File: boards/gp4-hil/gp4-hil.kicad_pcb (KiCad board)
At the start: 4 copper layers, 160 x 60 mm, 452 parts, among them J1 BEL_FUSE_0826-1G1T-23-F, J2 XILINX_JTAG, J3 XILINX_JTAG_ICESIDE, J4 XILINX_JTAG_ICESIDE, K1 CONN_3_PWROUT, P1 GPAK_ZIF, P2 2x10 HEADER, Q1 SSM6N58NU, Q11 SSM6N58NU, Q12 DMP2069UFY4, Q13 SSM6N58NU, Q14 SSM6N58NU, Q15 SSM6N58NU, Q16 SSM6N58NU, Q17 SSM6N58NU, Q18 SSM6N58NU, Q19 SSM6N58NU, Q20 SSM6N58NU, Q21 SSM6N58NU, Q22 DMP2069UFY4, U1 MIC2288-DFN, U10 AD9609, U11 DAC084S085, U12 DAC084S085, U13 DAC084S085, U14 DAC084S085, U15 TS3A4751, U16 TS3A4751, U17 TS3A4751, U18 TS3A4751, U19 TS3A4751, U2 XC7A100T-1FTG256C, U20 SIP32408, U21 SIP32408, U22 SIP32408, U23 SIP32408, U24 SIP32408, U25 TS3A4751, U26 TS3A4751, U27 TS3A4751, U28 TS3A4751, U29 TXB0104RUT, U3 LTC3374-QFN, U30 TXB0104RUT, U31 ADA4937-2, U32 SIP32408, U33 125 MHz, U34 INA199A2RSW, U35 INA199A2RSW, U36 INA199A2RSW, U4 SIP32408, U5 KSZ9031RN, U6 W25Q32FW, U7 25 MHz, U8 ADG726, U9 AD9609

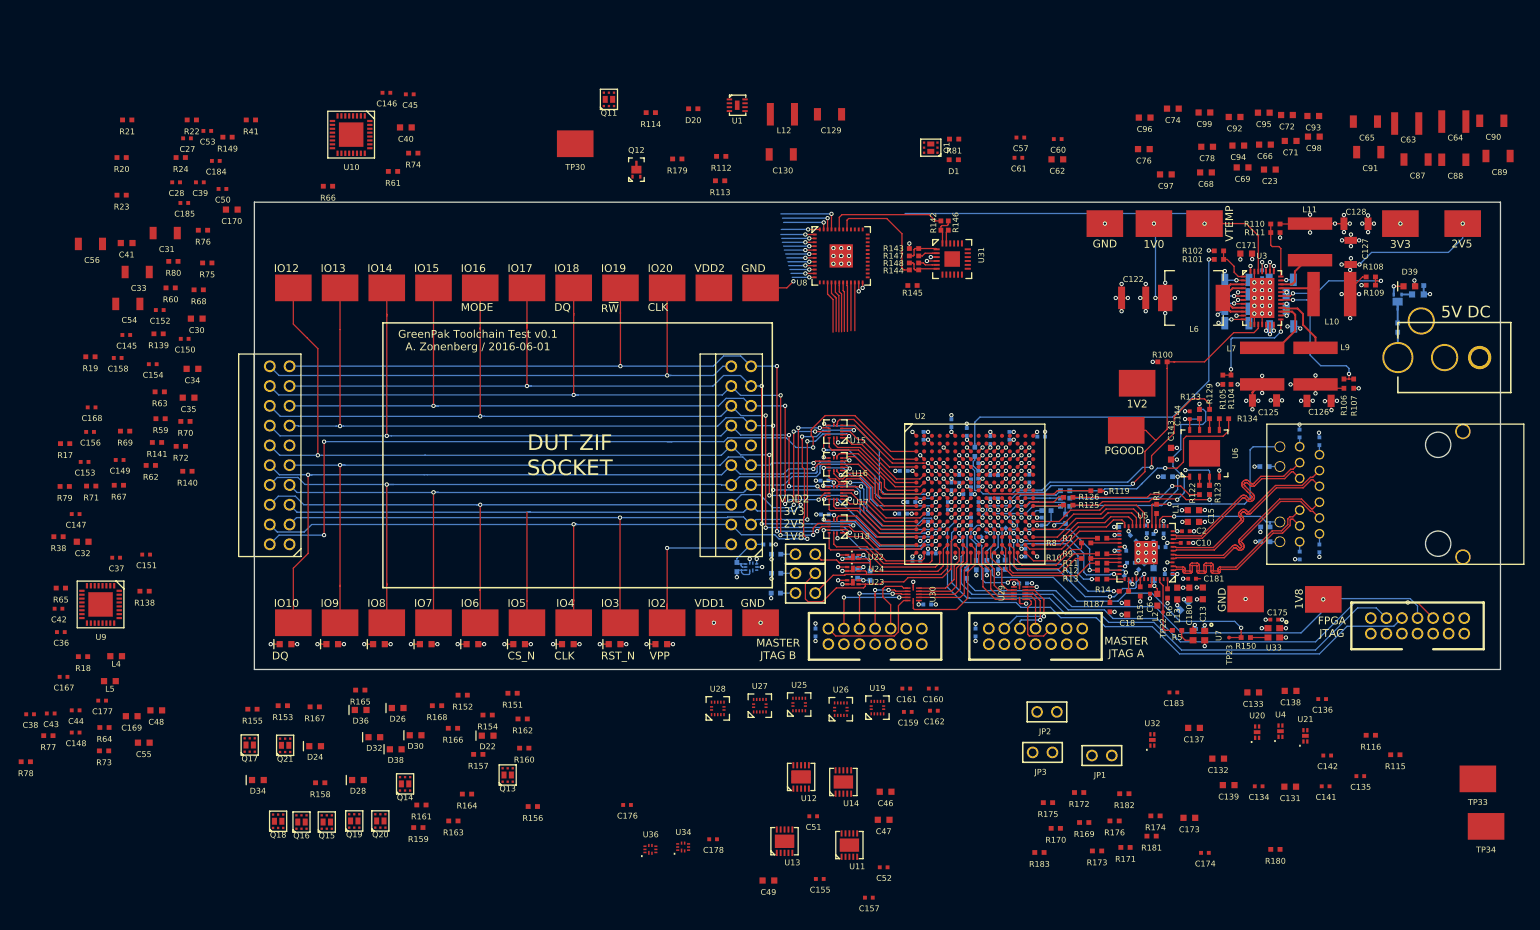
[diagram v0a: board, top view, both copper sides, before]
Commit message: Lots of decoupling capacitor placement
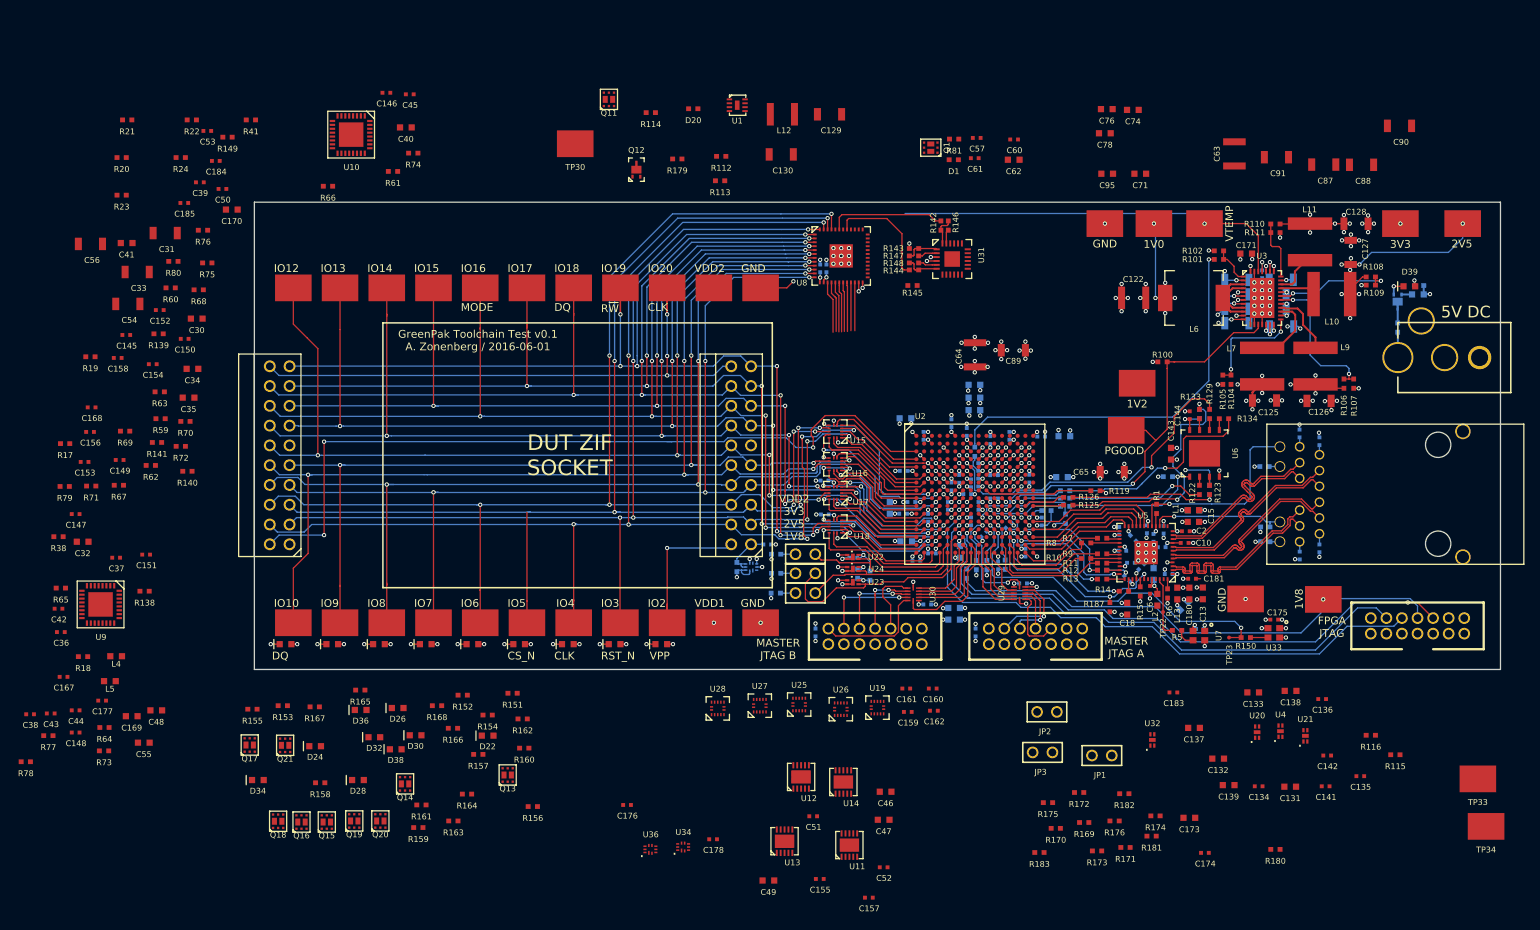
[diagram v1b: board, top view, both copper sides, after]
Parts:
- C23, C27, C28, C66, C68, C69, C72, C92, C93, C94, C96, C97, C98, C99: moved to B.Cu
- moved C28 84.2 mm to (94.5, 68.5), turned to 90 degrees
- moved C27 83.0 mm to (93.7, 68.5), turned to 90 degrees
- moved C92 72.9 mm to (111.6, 112.8), turned to 270 degrees
- moved C98 72.4 mm to (102.6, 99.2), turned to 90 degrees
- moved C96 68.5 mm to (110.1, 112.8), turned to 90 degrees
- moved C64 68.4 mm to (113.5, 79.6), turned to 270 degrees
- moved C89 67.0 mm to (118.5, 79.0)
- moved C94 66.3 mm to (104.7, 103.5)
- moved C68 58.1 mm to (111.6, 104.9), turned to 270 degrees
- moved C65 55.5 mm to (131.2, 94.7)
- moved C99 54.9 mm to (104.6, 87.8)
- moved C72 53.0 mm to (113.5, 83.5)
- moved C93 52.1 mm to (125.0, 90.0)
- moved C66 50.5 mm to (113.5, 86.7)
- moved C69 45.4 mm to (113.5, 85.1), turned to 180 degrees
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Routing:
- net /Analog IO/GND: track 933.1 -> 1006.5 mm, vias 160 -> 183
- net /Analog IO/DUT_GPIO5: track 103.0 -> 158.3 mm, vias 4 -> 6
- net /Analog IO/DUT_GPIO6: track 107.8 -> 162.8 mm, vias 5 -> 7
- net /Analog IO/DUT_GPIO4: track 112.0 -> 167.0 mm, vias 5 -> 7
- net /Analog IO/DUT_GPIO3: track 103.0 -> 155.5 mm, vias 5 -> 7
- net /Analog IO/DUT_GPIO10: track 97.5 -> 135.7 mm, vias 3 -> 5
- net /Analog IO/DUT_GPIO8: track 100.0 -> 136.9 mm, vias 3 -> 5
- net /Analog IO/DUT_GPIO12: track 109.0 -> 145.9 mm, vias 5 -> 7
- net /Analog IO/DUT_GPIO7: track 96.1 -> 132.7 mm, vias 3 -> 5
- net /Analog IO/DUT_GPIO14: track 103.2 -> 139.5 mm, vias 5 -> 7
- net /Analog IO/DUT_GPIO9: track 94.6 -> 130.7 mm, vias 3 -> 5
- net /Analog IO/DUT_GPIO16: track 113.5 -> 149.4 mm, vias 5 -> 7
- net /Analog IO/DUT_GPIO19: track 106.6 -> 142.0 mm, vias 5 -> 7
- net /Analog IO/DUT_GPIO18: track 111.8 -> 146.6 mm, vias 5 -> 7
- net /Analog IO/DUT_GPIO13: track 105.4 -> 139.4 mm, vias 5 -> 7
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
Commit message: Lots of layout on ADC A among other things
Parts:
- C167, C168, C36, C37, C38, C39, Q19, Q20, R138, R139, R151, R153, R155, R157, R159, R161, R163, R165, R167: moved to B.Cu
- R144, R145, R148, R149: value 100K 0.1% -> 10K 0.1%
- moved C38 142.1 mm to (119.8, 63.3), turned to 270 degrees
- moved C36 132.2 mm to (119.0, 66.2)
- moved U9 128.2 mm to (121.0, 65.9), turned to 180 degrees
- moved C169 124.1 mm to (112.3, 63.1)
- moved C167 123.3 mm to (106.9, 66.0), turned to 270 degrees
- moved C37 121.7 mm to (118.9, 67.7)
- moved R138 117.7 mm to (116.0, 65.8), turned to 180 degrees
- moved C168 107.4 mm to (105.9, 68.0), turned to 90 degrees
- moved C39 107.4 mm to (120.8, 68.4), turned to 90 degrees
- moved R139 107.2 mm to (115.8, 73.6), turned to 180 degrees
- moved R149 93.6 mm to (109.0, 71.5), turned to 270 degrees
- moved C170 93.5 mm to (111.0, 71.5)
- moved U10 90.4 mm to (121.0, 73.7), turned to 180 degrees
- moved C178 90.4 mm to (93.8, 52.5)
- moved U34 90.4 mm to (90.0, 53.5)
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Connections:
- Q11 pad G2: /Analog IO/DUT_GPIO9 -> /Analog IO/DUT_GPIO19
- Q18 pad G1: /Analog IO/DUT_GPIO7 -> /Analog IO/DUT_GPIO18
- Q19 pad G1: /Analog IO/DUT_GPIO8 -> /Analog IO/DUT_GPIO7
- Q19 pad G2: /Analog IO/DUT_GPIO18 -> /Analog IO/DUT_GPIO8
- Q20 pad G1: /Analog IO/DUT_GPIO19 -> /Analog IO/DUT_GPIO9
- R161 pad 1: Net-(Q18-PadD1) -> Net-(Q19-PadD1)
- R163 pad 1: Net-(Q19-PadD1) -> Net-(Q19-PadD2)
- R164 pad 1: Net-(Q19-PadD2) -> Net-(Q18-PadD1)
- R165 pad 1: Net-(Q11-PadD2) -> Net-(Q20-PadD1)
- R166 pad 1: Net-(Q20-PadD1) -> Net-(Q11-PadD2)
- U8 pad 29: /Analog IO/PSU_VTEMP -> /Analog IO/ADC_GPIO2
- U8 pad 30: /Analog IO/ADC_GPIO2 -> /Analog IO/ADC_GPIO20
- U8 pad 31: /Analog IO/ADC_GPIO20 -> /Analog IO/ADC_VDD1
- U8 pad 32: /Analog IO/ADC_VDD1 -> /Analog IO/ADC_VDD2
- U8 pad 33: /Analog IO/ADC_VDD2 -> /Analog IO/PSU_VTEMP
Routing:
- net /Analog IO/GND: track 1006.5 -> 1075.0 mm, vias 183 -> 205
- net /Analog IO/A3V3: track 6.83 -> 35.7 mm, vias 5 -> 11
- net /Analog IO/A1V8: track 0.00 -> 14.2 mm, vias 0 -> 4
- net /Analog IO/ADC_B_P: track 0.00 -> 12.2 mm
- net /Analog IO/ADC_B_N: track 0.00 -> 12.0 mm
- net /Analog IO/ADC_B_VCM: track 0.00 -> 11.5 mm, vias 0 -> 2
- net /Analog IO/ADC_A_P: track 0.00 -> 10.2 mm
- net /Analog IO/ADC_A_N: track 0.00 -> 10.2 mm
- net /Analog IO/ADC_A_VCM: track 0.00 -> 8.14 mm, vias 0 -> 2
- net /Analog IO/DUT_GPIO9: track 130.7 -> 138.6 mm, vias 5 -> 6
- net /Analog IO/PSU_VTEMP: track 51.1 -> 58.5 mm, vias 1 -> 2
- net Net-(Q20-PadD2): track 0.00 -> 6.50 mm
- net Net-(Q19-PadD2): track 0.00 -> 4.93 mm
- net Net-(Q19-PadD1): track 0.00 -> 4.88 mm
- net Net-(Q20-PadD1): track 0.00 -> 4.84 mm
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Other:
- board text added: "GreenPak Toolchain Test v0.1 A. Zonenberg / 2016-06-03"
- board text added: "VDD1 3V3 2V5 1V8"
- board text removed: "GreenPak Toolchain Test v0.1 A. Zonenberg / 2016-06-01"

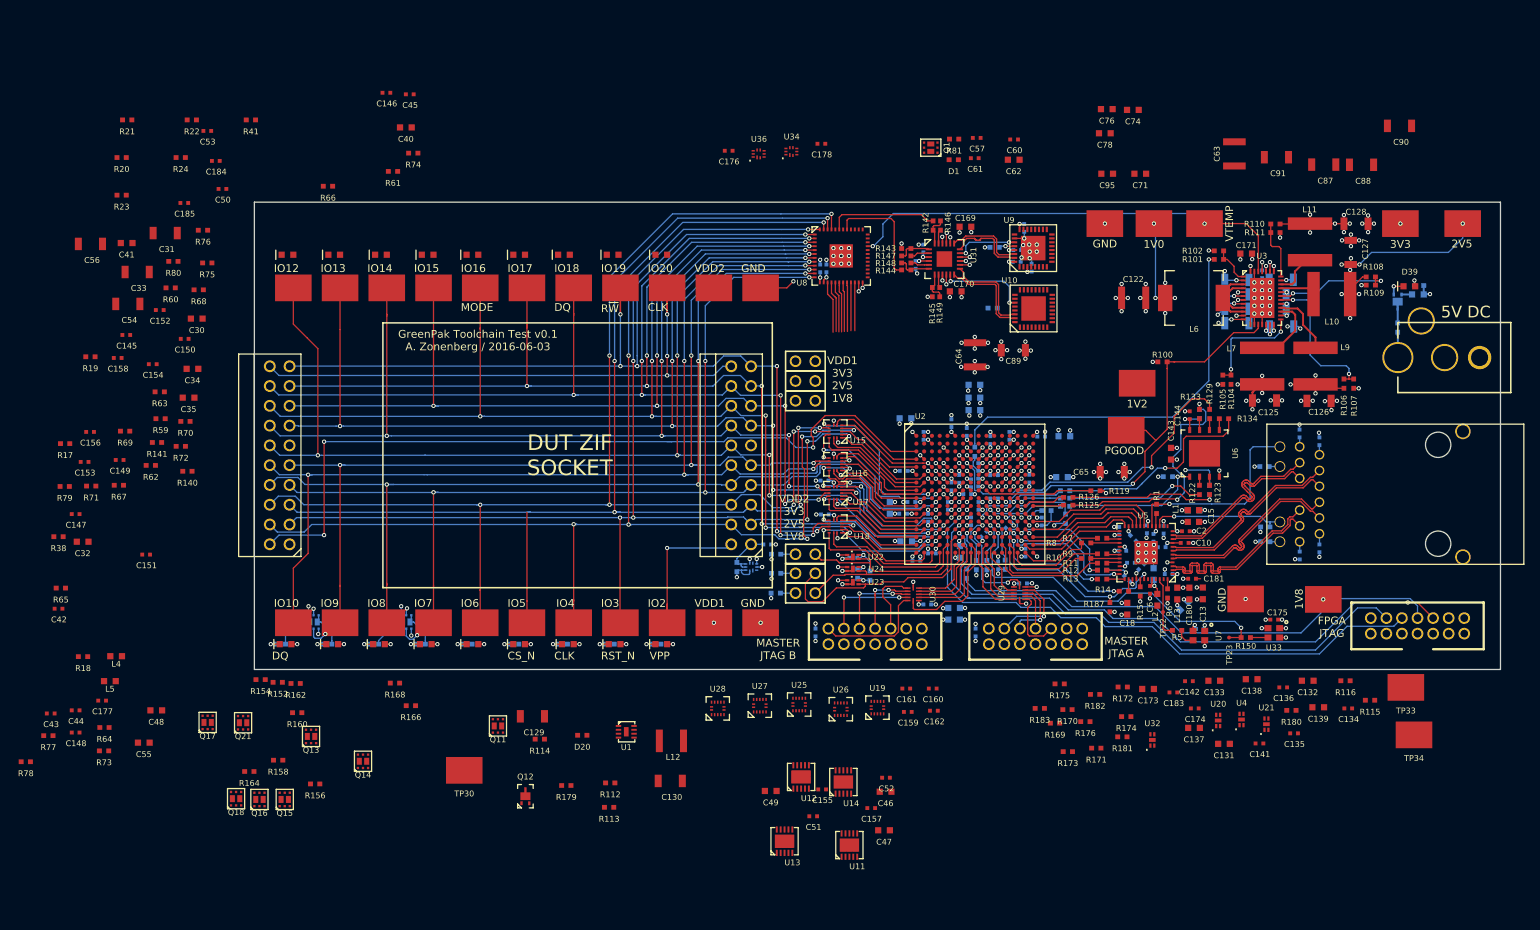
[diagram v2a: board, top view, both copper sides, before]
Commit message: More ADC layout
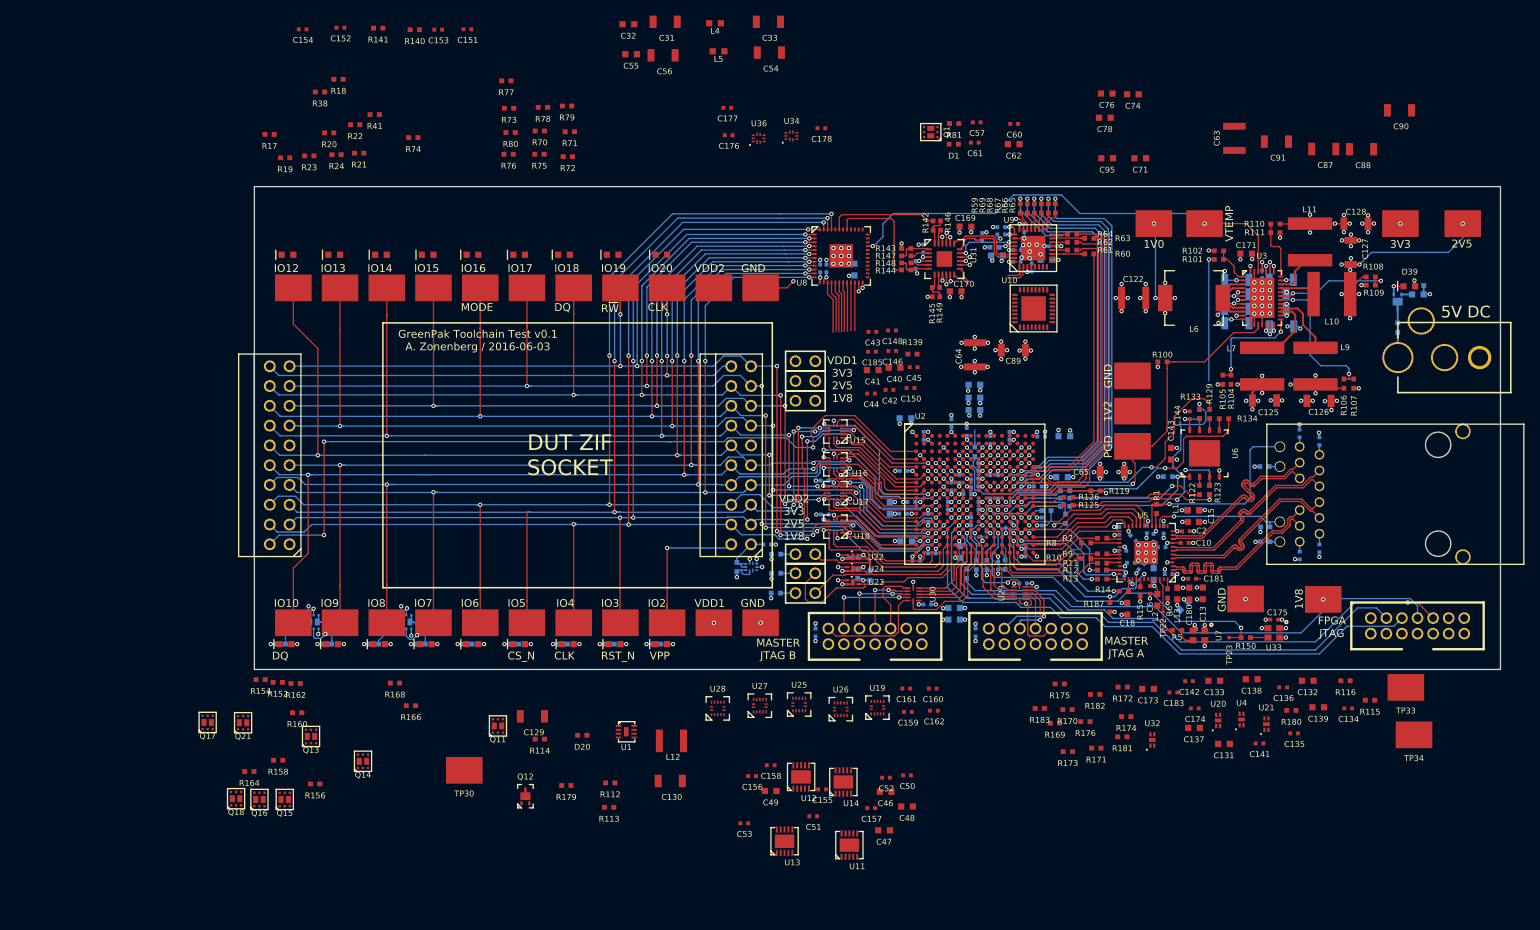
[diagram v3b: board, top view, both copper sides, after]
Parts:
- C145, C147, C149, C184, C30, C34, C35: moved to B.Cu
- R139: moved to F.Cu
- moved R64 139.5 mm to (126.0, 64.1), turned to 180 degrees
- moved R65 136.7 mm to (123.8, 60.8), turned to 270 degrees
- moved C147 124.4 mm to (116.9, 63.2), turned to 180 degrees
- moved R67 123.7 mm to (122.0, 60.8), turned to 270 degrees
- moved R62 121.7 mm to (126.0, 65.2), turned to 180 degrees
- moved R63 121.0 mm to (128.2, 64.7), turned to 180 degrees
- moved R69 119.3 mm to (120.2, 60.8), turned to 270 degrees
- moved R60 118.0 mm to (128.2, 66.7), turned to 180 degrees
- moved C148 116.8 mm to (102.9, 76.5)
- moved C43 116.3 mm to (100.3, 76.7)
- moved C50 115.7 mm to (104.8, 133.6)
- moved C149 114.4 mm to (114.5, 64.5), turned to 90 degrees
- moved R59 113.7 mm to (119.3, 60.8), turned to 270 degrees
- moved C145 113.1 mm to (116.9, 64.2), turned to 180 degrees
- moved C53 112.5 mm to (83.9, 139.8)
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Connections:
- U2 pad A13: /Analog IO/ADC_B_D5 -> Net-(C151-Pad1)
- U2 pad A14: /Analog IO/ADC_B_D6 -> Net-(C152-Pad1)
- U2 pad B16: Net-(C152-Pad1) -> Net-(C154-Pad1)
- U2 pad C16: Net-(C151-Pad1) -> Net-(C153-Pad1)
- U2 pad D11: /Analog IO/ADC_A_D1 -> /Analog IO/DAC_B_DIN
- U2 pad D14: /Analog IO/ADC_A_D2 -> /Analog IO/DAC_SCLK
- U2 pad D15: /Analog IO/ADC_A_D3 -> /Analog IO/DAC_SYNC_N
- U2 pad D16: /Analog IO/ADC_A_D7 -> /Analog IO/ADC_B_D6
- U2 pad E11: /Analog IO/ADC_A_D0 -> /Analog IO/DAC_A_DIN
- U2 pad E15: /Analog IO/ADC_A_D9 -> /Analog IO/ADC_B_D5
- U2 pad E16: /Analog IO/ADC_A_D6 -> /Analog IO/ADC_A_D0
- U2 pad F12: /Analog IO/ADC_A_D4 -> /Analog IO/DAC_D_DIN
- U2 pad F13: /Analog IO/ADC_A_D5 -> /Analog IO/ADC_B_MODE
- U2 pad F14: /Analog IO/DAC_B_DIN -> /Analog IO/ADC_A_D9
- U2 pad F15: /Analog IO/ADC_A_D8 -> /Analog IO/ADC_A_D1
- U2 pad G12: Net-(C154-Pad1) -> /Analog IO/ADC_A_D8
- U2 pad G14: /Analog IO/DAC_C_DIN -> /Analog IO/ADC_A_D7
- U2 pad G15: /Analog IO/DAC_SCLK -> /Analog IO/ADC_A_D2
- U2 pad G16: /Analog IO/DAC_SYNC_N -> /Analog IO/ADC_A_D3
- U2 pad H11: Net-(C153-Pad1) -> /Analog IO/DAC_C_DIN
- U2 pad H13: /Analog IO/DAC_D_DIN -> /Analog IO/ADC_A_D6
- U2 pad H14: /Analog IO/ADC_B_MODE -> /Analog IO/ADC_A_D5
- U2 pad H16: /Analog IO/DAC_A_DIN -> /Analog IO/ADC_A_D4
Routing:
- net /Analog IO/ADC_A_D6: track 0.00 -> 54.0 mm, vias 0 -> 2
- net /Analog IO/ADC_A_D8: track 0.00 -> 53.7 mm, vias 0 -> 2
- net /Analog IO/ADC_A_D5: track 0.71 -> 53.5 mm, vias 1 -> 2
- net /Analog IO/ADC_A_D7: track 0.00 -> 52.2 mm, vias 0 -> 2
- net /Analog IO/ADC_A_D9: track 0.71 -> 50.9 mm, vias 1 -> 2
- net /Analog IO/ADC_A_D4: track 0.71 -> 44.6 mm, vias 1 -> 0
- net /Analog IO/ADC_A_D2: track 0.71 -> 42.2 mm, vias 1 -> 0
- net /Analog IO/ADC_A_D3: track 0.71 -> 40.5 mm, vias 1 -> 0
- net /Analog IO/ADC_A_D1: track 0.71 -> 38.8 mm, vias 1 -> 0
- net /Power supply/1V0_VSENSE: track 51.2 -> 18.5 mm
- net /Analog IO/ADC_A_D0: track 0.71 -> 33.2 mm, vias 1 -> 0
- net /Analog IO/GND: track 1075.0 -> 1086.6 mm, vias 205 -> 210
- net /Analog IO/ADC_B_VCM: track 11.5 -> 1.26 mm, vias 2 -> 1
- net /Analog IO/ADC_B_P: track 12.2 -> 2.31 mm
- net /Analog IO/ADC_B_N: track 12.0 -> 2.18 mm
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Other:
- board size 160 x 60 mm -> 160 x 62 mm
- board text added: "PGD"
- board text removed: "PGOOD"
